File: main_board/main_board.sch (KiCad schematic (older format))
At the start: 0 parts

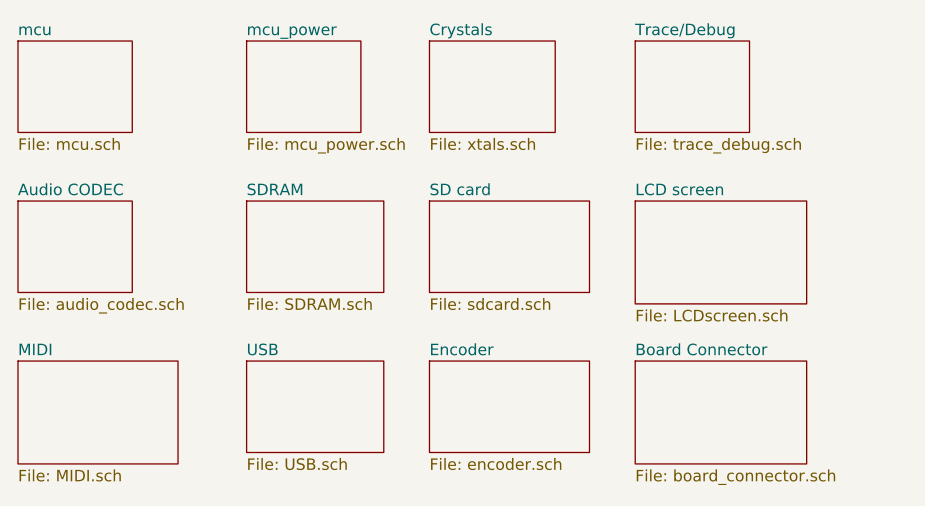
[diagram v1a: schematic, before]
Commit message: Added MIDI connectors and SD card to io_board
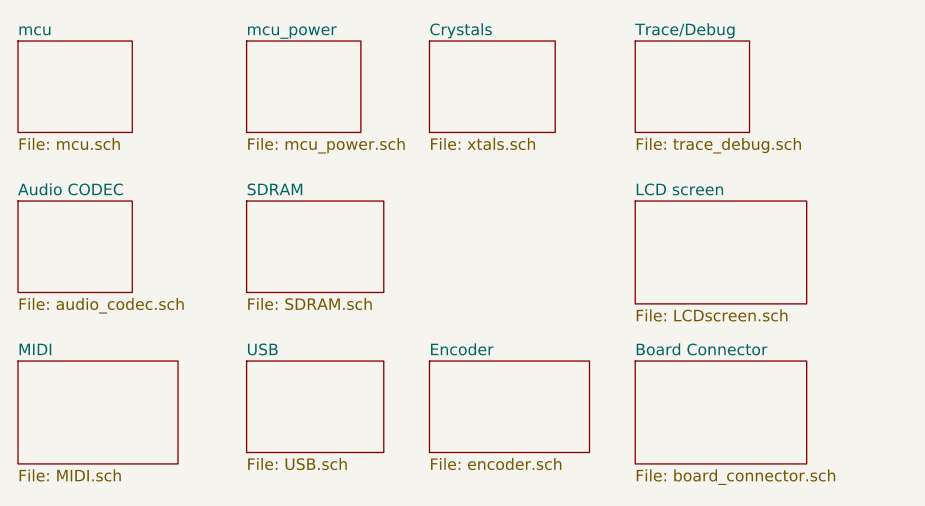
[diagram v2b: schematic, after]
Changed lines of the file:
@@
 EESchema Schematic File Version 4
 LIBS:main_board-cache
-EELAYER 26 0
+EELAYER 29 0
 EELAYER END
 $Descr A4 11693 8268
 encoding utf-8
-Sheet 1 13
+Sheet 1 12
 Title "MIDI Studio Schematic"
 Date ""
@@
 $EndSheet
 $Sheet
-S 2900 1500 700  400
-U 5CFEB435
-F0 "SD card" 50
-F1 "sdcard.sch" 50
-$EndSheet
-$Sheet
